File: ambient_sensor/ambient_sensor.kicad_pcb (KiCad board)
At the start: 2 copper layers, 15.2 x 17.8 mm, 2 parts

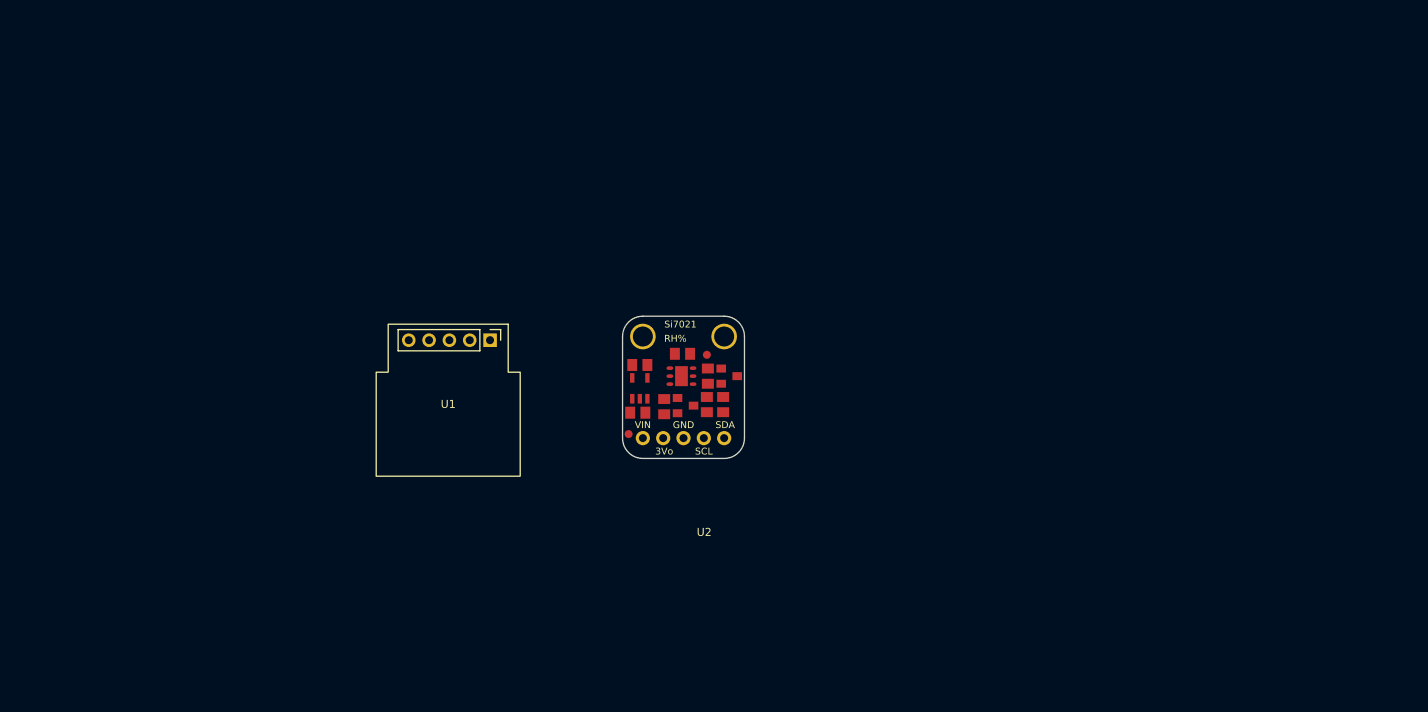
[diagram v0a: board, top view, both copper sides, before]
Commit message: footprint and schematic for BMP280
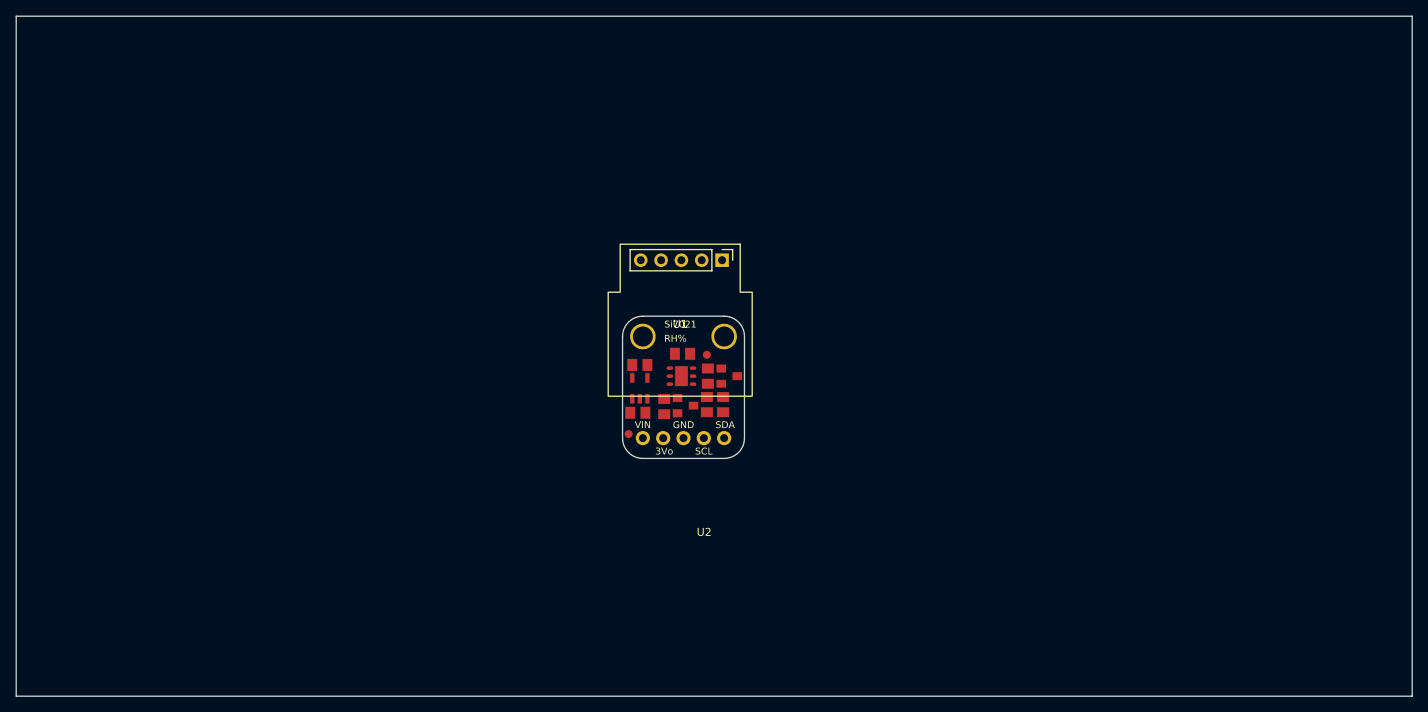
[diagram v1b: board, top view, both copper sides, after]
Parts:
- moved U1 30.7 mm to (150.5, 71.0)
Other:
- board size 15.2 x 17.8 mm -> 174.5 x 85 mm
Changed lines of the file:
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@@
 	(footprint "sensors:SGP30"
 		(layer "F.Cu")
-		(at 121.5 81)
+		(at 150.5 71)
 		(property "Reference" "U1"
 			(at 3 -5.5 0)
@@
 		)
 	)
+	(gr_rect
+		(start 70.5 27)
+		(end 245 112)
+		(stroke
+			(width 0.05)
+			(type default)
+		)
+		(fill none)
+		(layer "Edge.Cuts")
+	)
 )

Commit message: last modification in schema for now
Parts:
- added U3: ~, sensors:BMP280, F.Cu at (124.0, 75.9)
- added U4: ATmega328-P, Package_DIP:DIP-28_W7.62mm, F.Cu at (96.4, 45.5)
- moved U2 24.8 mm to (173.9, 74.3)

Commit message: clock
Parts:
- added Y1: Crystal, Crystal:Resonator-2Pin_W10.0mm_H5.0mm, F.Cu at (139.5, 83.0)

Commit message: C and R
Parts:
- added C1: C, Capacitor_SMD:C_1206_3216Metric, F.Cu at (187.1, 78.7)
- added R2: 4.7k, Resistor_SMD:R_1206_3216Metric, F.Cu at (187.0, 82.0)
- moved Y1 16.0 mm to (155.5, 84.0)
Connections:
- U1 pad 1: unconnected-(U1-2-6V-Pad1) -> 5v
- U1 pad 2: unconnected-(U1-SDA-Pad2) -> Net-(U1-SDA)
- U1 pad 3: unconnected-(U1-SCL-Pad3) -> Net-(U1-SCL)
- U1 pad 5: unconnected-(U1-GND-Pad5) -> GND
- U3 pad 1: unconnected-(U3-VIN-Pad1) -> 5v
- U3 pad 2: unconnected-(U3-3Vo-Pad2) -> 5v
- U3 pad 3: unconnected-(U3-GND-Pad3) -> GND
- U3 pad 5: unconnected-(U3-SDO-Pad5) -> Net-(U1-SCL)
- U3 pad 6: unconnected-(U3-SDI-Pad6) -> Net-(U1-SDA)
- U4 pad 20: unconnected-(U4-AVCC-Pad20) -> 5v
- U4 pad 22: Net-(U4-GND-Pad22) -> GND
- U4 pad 27: unconnected-(U4-PC4-Pad27) -> Net-(U2-SDA)
- U4 pad 28: unconnected-(U4-PC5-Pad28) -> Net-(U1-SCL)
- U4 pad 7: unconnected-(U4-VCC-Pad7) -> 5v
- U4 pad 8: Net-(U4-GND-Pad22) -> GND

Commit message: clock
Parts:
- added C2: 22p, Capacitor_SMD:C_1206_3216Metric, F.Cu at (157.0, 91.5)
- C1: value C -> 22p
- moved U2 19.0 mm to (192.9, 73.8)
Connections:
- C1 pad 2: unconnected-(C1-Pad2) -> GND
- U4 pad 10: unconnected-(U4-XTAL2/PB7-Pad10) -> unconnected-(C2-Pad1)
- U4 pad 9: unconnected-(U4-XTAL1/PB6-Pad9) -> unconnected-(C1-Pad1)
- Y1 pad 1: unconnected-(Y1-Pad1) -> unconnected-(C2-Pad1)
- Y1 pad 2: unconnected-(Y1-Pad2) -> unconnected-(C1-Pad1)

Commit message: addittional components
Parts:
- added U6: LD1117S33TR_SOT223, Package_TO_SOT_SMD:SOT-223-3_TabPin2, F.Cu at (189.8, 69.0)

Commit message: clock and reset
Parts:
- added C3: 10u, Capacitor_SMD:C_1206_3216Metric, F.Cu at (108.0, 62.0)
- added J1: Conn_01x02_Pin, Connector_PinHeader_2.54mm:PinHeader_1x02_P2.54mm_Vertical, F.Cu at (93.5, 42.7)
- added R3: 10k, Resistor_SMD:R_1206_3216Metric, F.Cu at (88.5, 45.0)
- moved C1 106.0 mm to (82.0, 64.5)
- moved C2 78.7 mm to (81.5, 69.5)
- moved Y1 68.1 mm to (89.0, 69.5), turned to 90 degrees
- moved R2 56.4 mm to (137.5, 55.0)
- moved U3 22.2 mm to (136.2, 57.4)
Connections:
- U1 pad 1: 5v -> +4V
- U3 pad 1: 5v -> +4V
- U3 pad 2: 5v -> +4V
- U4 pad 20: 5v -> +4V
- U4 pad 21: unconnected-(U4-AREF-Pad21) -> +4V
- U4 pad 7: 5v -> +4V
- U6 pad 1: unconnected-(U6-GND-Pad1) -> GND
- U6 pad 2: unconnected-(U6-VO-Pad2) -> +4V

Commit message: sensors connected
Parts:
- added BT1: Battery, Battery:BatteryHolder_Keystone_2479_3xAAA, F.Cu at (191.8, 76.0)
- moved U2 57.0 mm to (140.5, 96.2)
- moved U6 24.3 mm to (172.7, 51.8)
- moved C1 8.53 mm to (73.5, 65.5)
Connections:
- U1 pad 2: Net-(U1-SDA) -> SDA
- U1 pad 3: Net-(U1-SCL) -> SCL
- U3 pad 2: +4V -> unconnected-(U3-3Vo-Pad2)
- U3 pad 4: unconnected-(U3-SCK-Pad4) -> SCL
- U3 pad 5: Net-(U1-SCL) -> unconnected-(U3-SDO-Pad5)
- U3 pad 6: Net-(U1-SDA) -> SDA
- U4 pad 27: Net-(U2-SDA) -> SDA
- U4 pad 28: Net-(U1-SCL) -> SCL
- U6 pad 3: unconnected-(U6-VI-Pad3) -> Net-(BT1-+)
